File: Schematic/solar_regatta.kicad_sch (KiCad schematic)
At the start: 21 parts, among them M1 24V, SW1 3_Pos_Switch, SW2 Deadman_Switch, SW3 Momentary_Throttle, U1 ESP32-S3, U2 NLSV2T244D

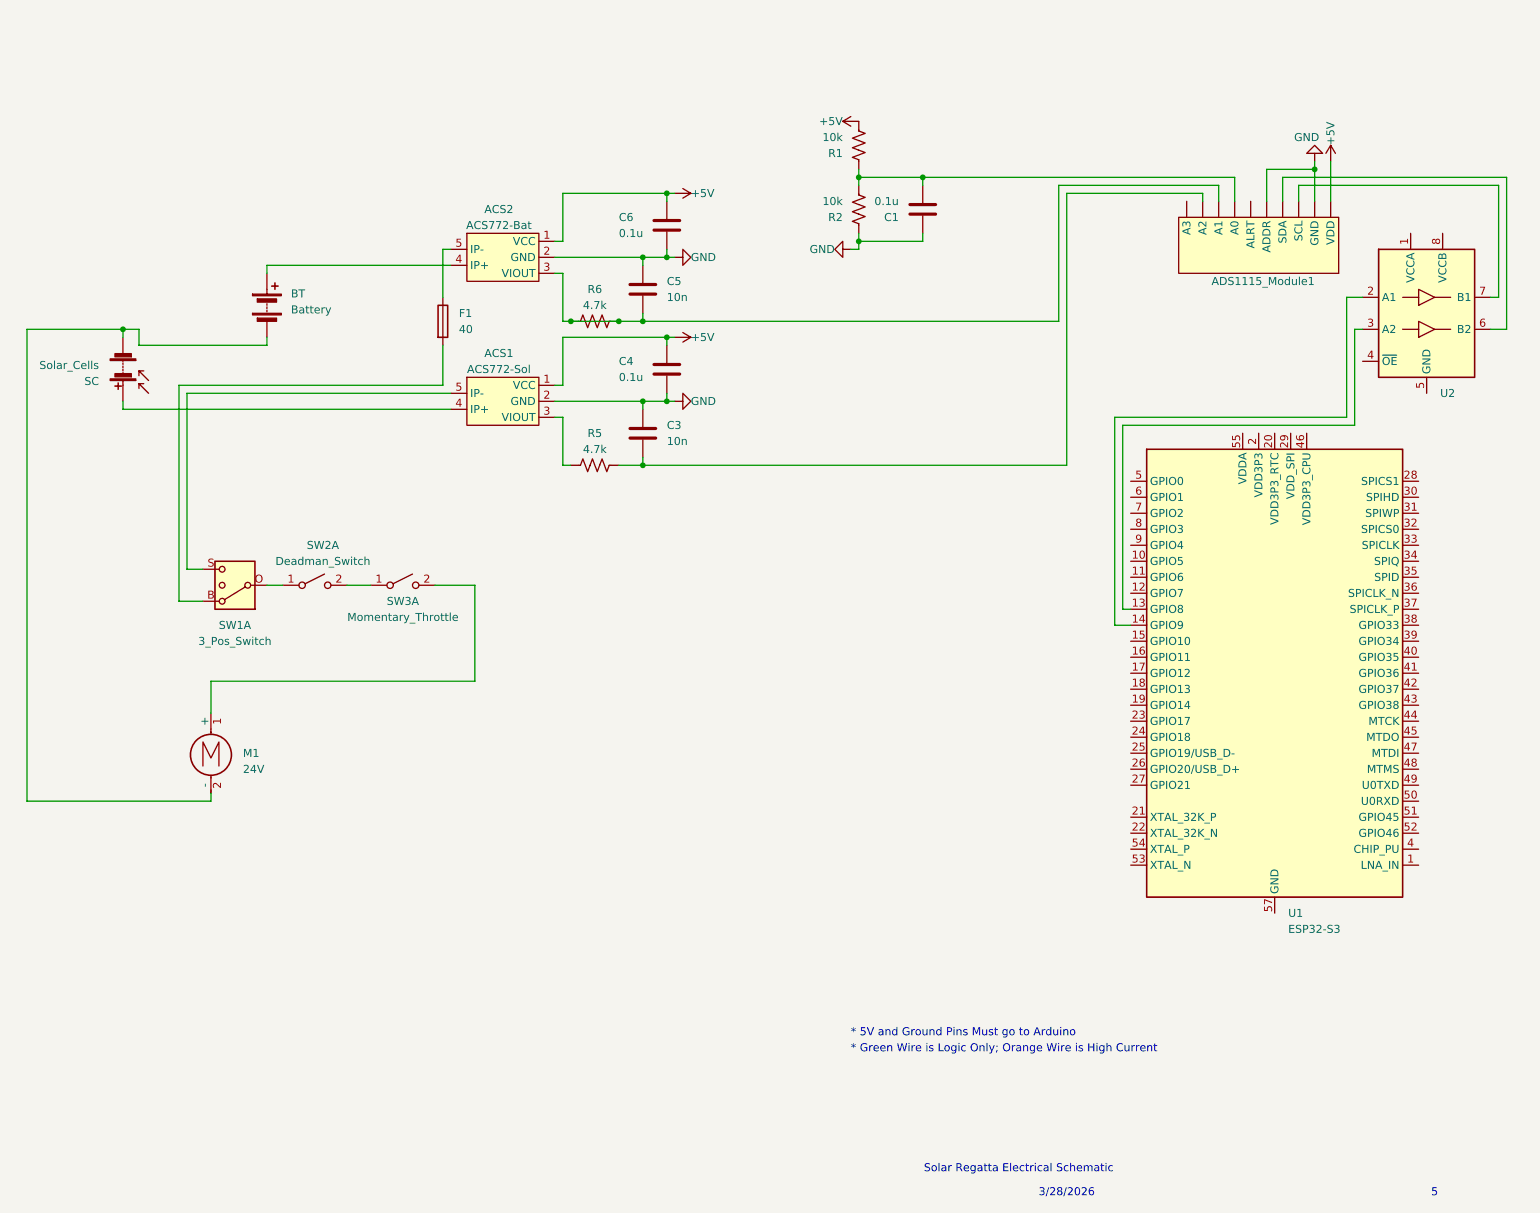
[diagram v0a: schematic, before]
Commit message: Update schematic to include complete esp32 system
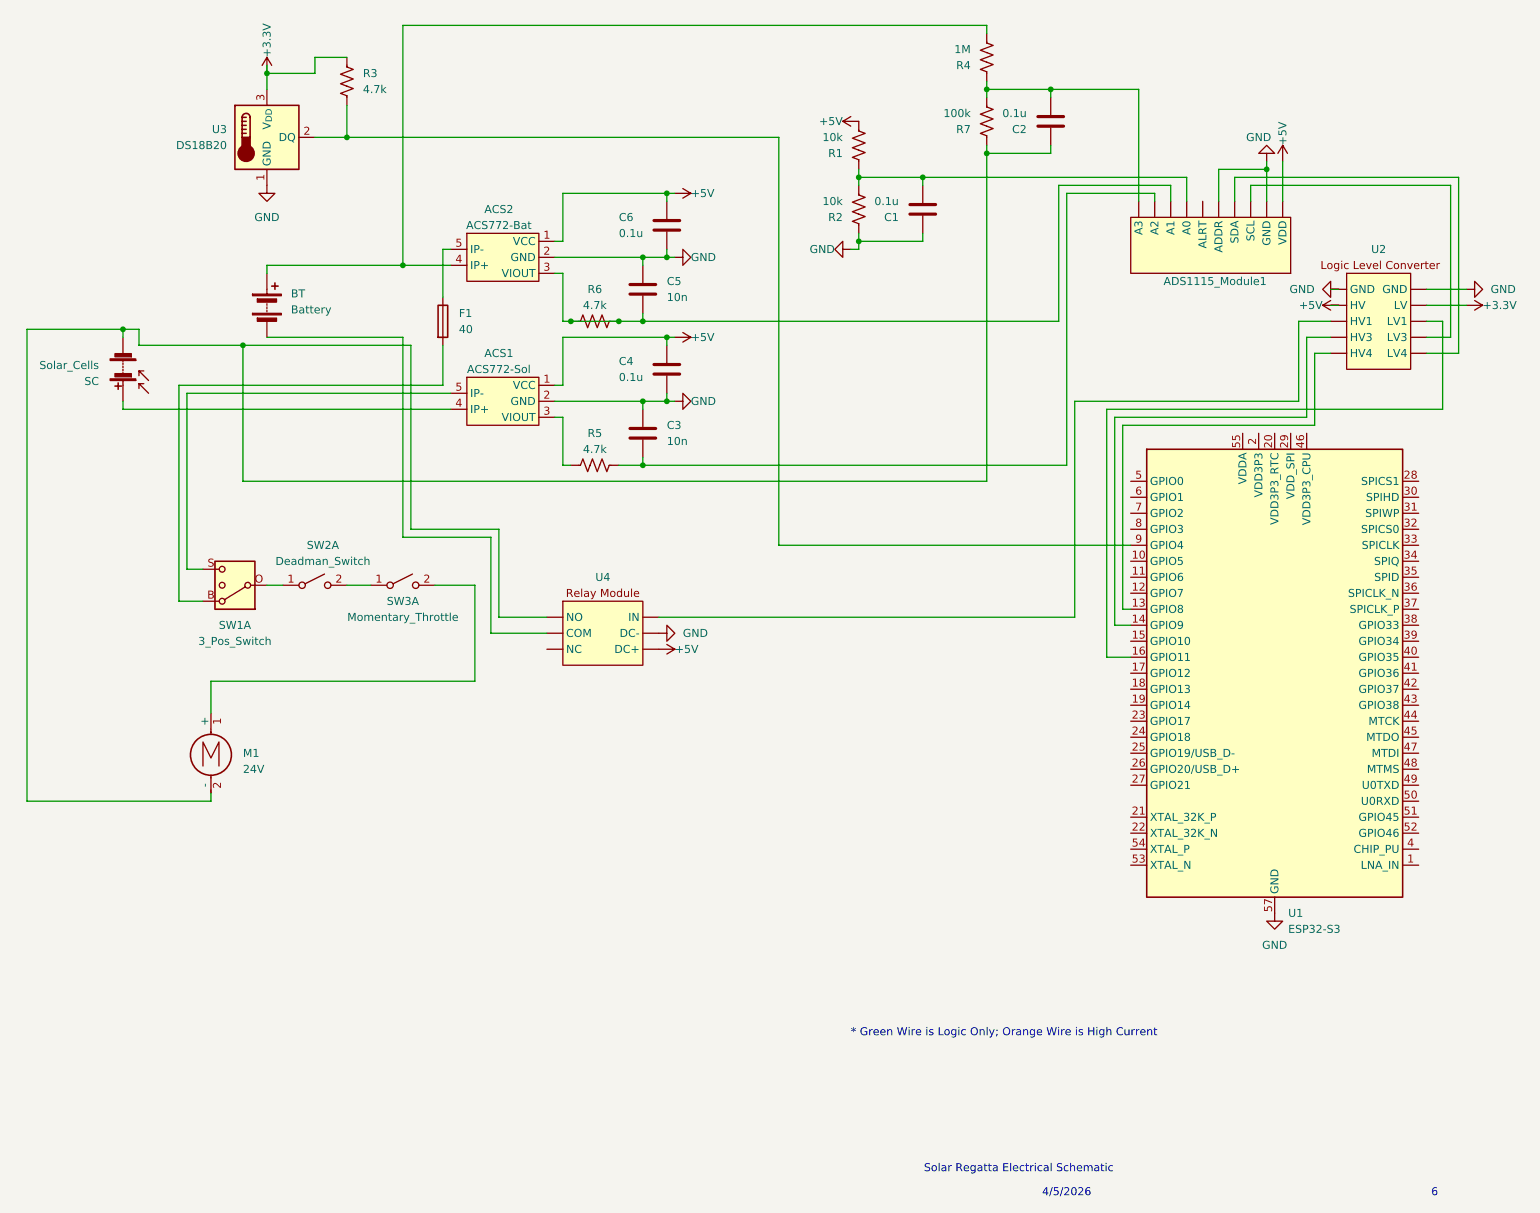
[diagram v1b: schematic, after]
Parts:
- removed U2: NLSV2T244D, Package_SO:SOIC-8_3.9x4.9mm_P1.27mm, symbol Logic_LevelTranslator:NLSV2T244D
- added C2: 0.1u, symbol Device:C
- added R3: 4.7k, symbol Device:R_US
- added R4: 1M, symbol Device:R_US
- added R7: 100k, symbol Device:R_US
- added U2: ~, symbol Custom_Library:LevelConverter
- added U3: DS18B20, Package_TO_SOT_THT:TO-92_Inline, symbol Sensor_Temperature:DS18B20
- added U4: ~, symbol Custom_Library:RelayModule
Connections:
- net +5V: now also U2. (LV4), U4. (DC+)
- net GND: now also U1.57 (GND), U2. (LV4), U3.1 (GND), U4. (DC+)
- net at ACS2.4 (IP+), BT.1 (+): now also R4.2
- net at M1.2 (-), SC.2 (-): now also C2.1, R7.1, U4. (DC+); no longer BT.2 (-)
- net at U1.13 (GPIO8): now also U2. (LV4)
- net at U1.14 (GPIO9): now also U2. (LV4)
- net at U1.16 (GPIO11): now also U2. (LV4)
- net at U1.9 (GPIO4): now also R3.2, U3.2 (DQ)
- new net: BT.2 (-), U4. (DC+)
- new net: ADS1115_Module1. (A3), C2.2, R4.1, R7.2
- new net: U2. (LV4), U4. (DC+)
- new net: ADS1115_Module1. (A3), U2. (LV4) (x2)
- new net +3.3V: R3.1, U2. (LV4), U3.3 (V_{DD})
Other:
- note added: "4/5/2026"
- note added: "6"
- note removed: "* 5V and Ground Pins Must go to Arduino"
- note removed: "3/28/2026"
- note removed: "5"
- moved on the sheet: ADS1115_Module1

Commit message: Remove temp, relays from schematic
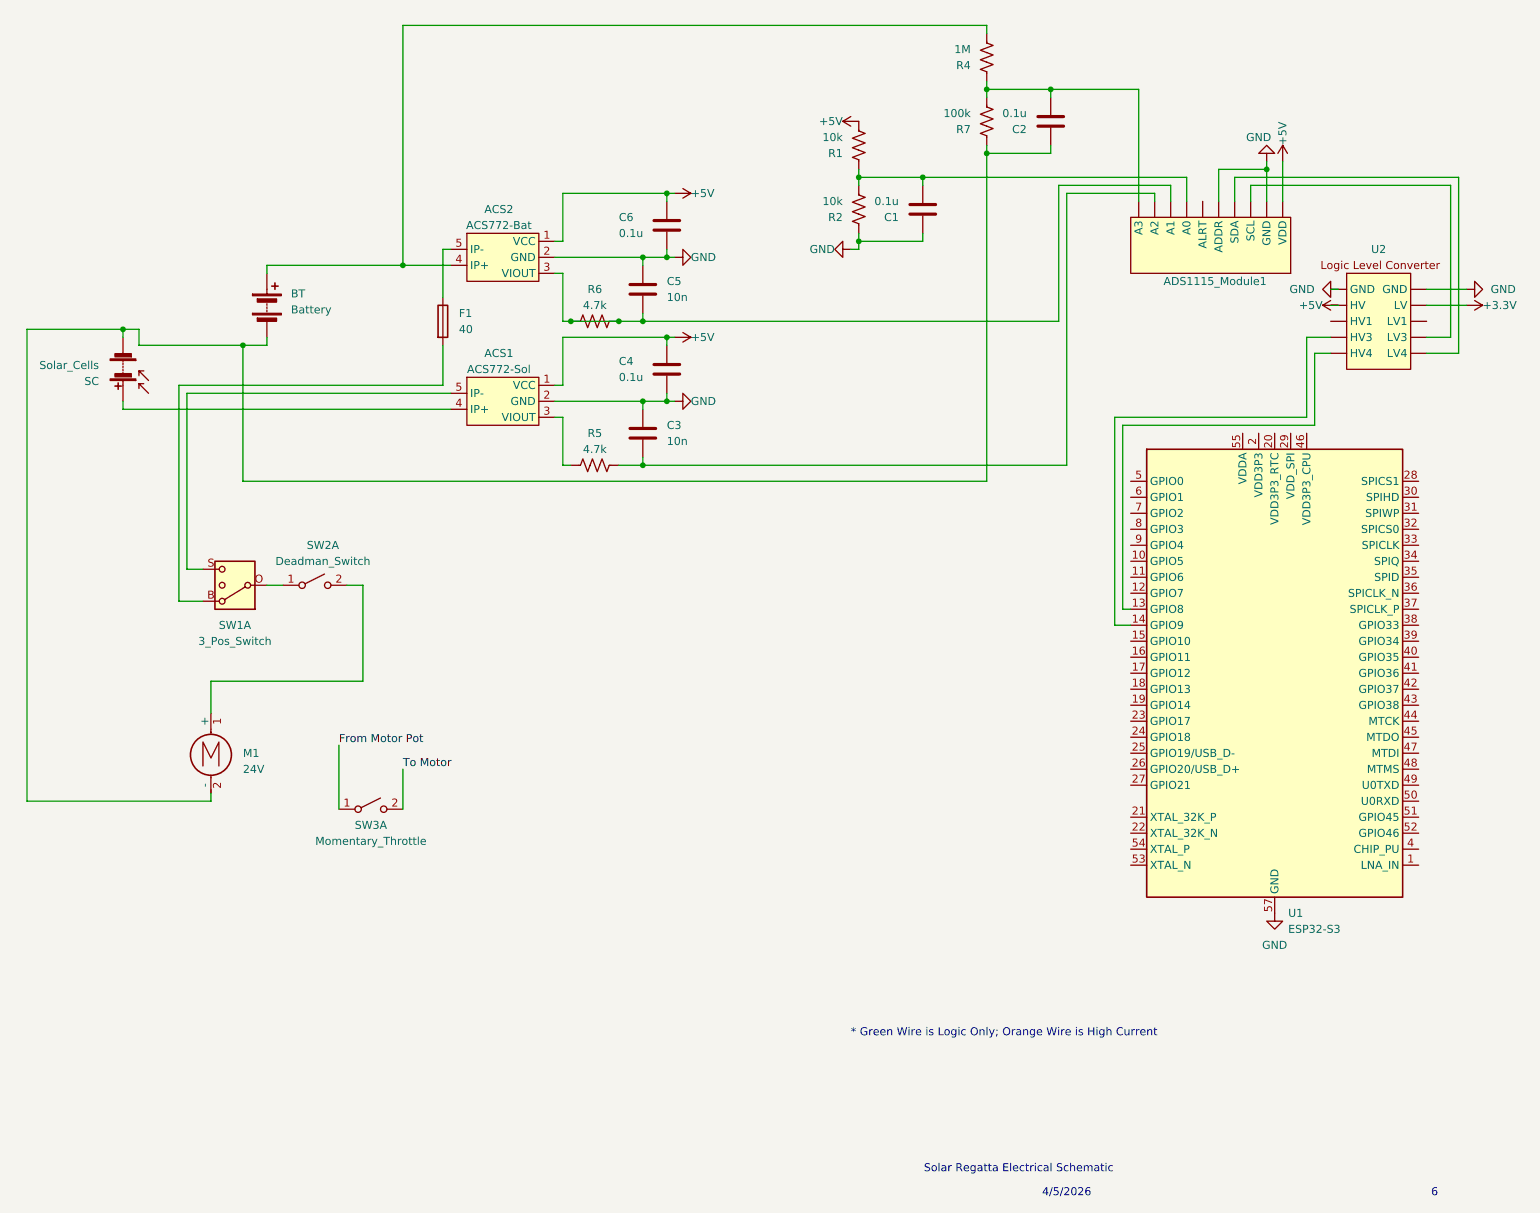
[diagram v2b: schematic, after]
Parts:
- removed R3: 4.7k, symbol Device:R_US
- removed U3: DS18B20, Package_TO_SOT_THT:TO-92_Inline, symbol Sensor_Temperature:DS18B20
- removed U4: ~, symbol Custom_Library:RelayModule
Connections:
- net at BT.2 (-): now also C2.1, M1.2 (-), R7.1, SC.2 (-)
- net at SW2.2 (B): now also M1.1 (+); no longer SW3.1 (A)
- net To Motor: now reaches SW3.2 (B)
- net To Motor: no longer M1.1 (+)
- net at U1.16 (GPIO11): no longer U2. (LV4)
- new net: ADS1115_Module1. (A3), U2. (LV4) (x2)
- new net From Motor Pot: SW3.1 (A)
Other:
- moved on the sheet: SW3A

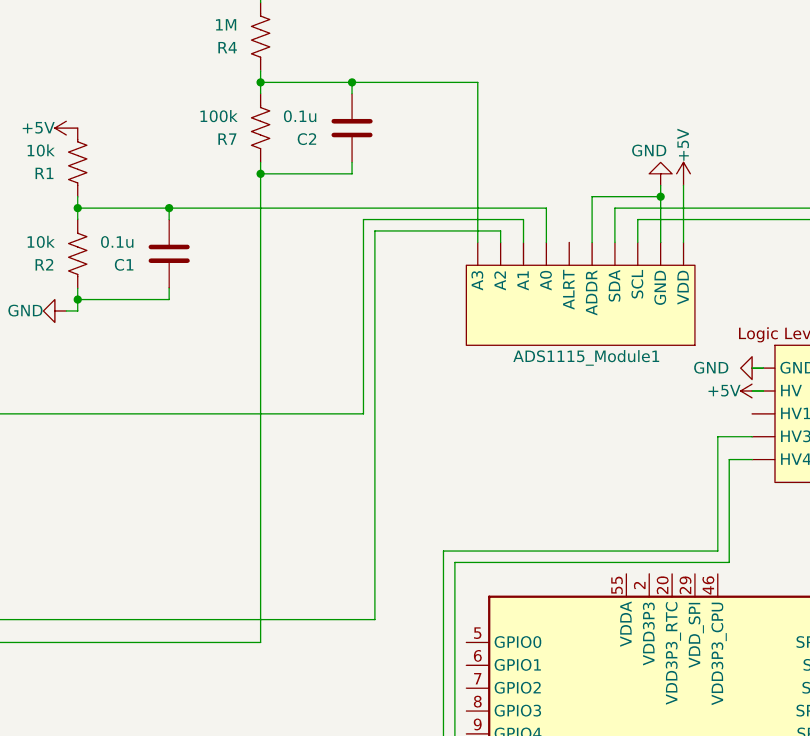
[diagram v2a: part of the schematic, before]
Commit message: Update schematic; Add Models directory
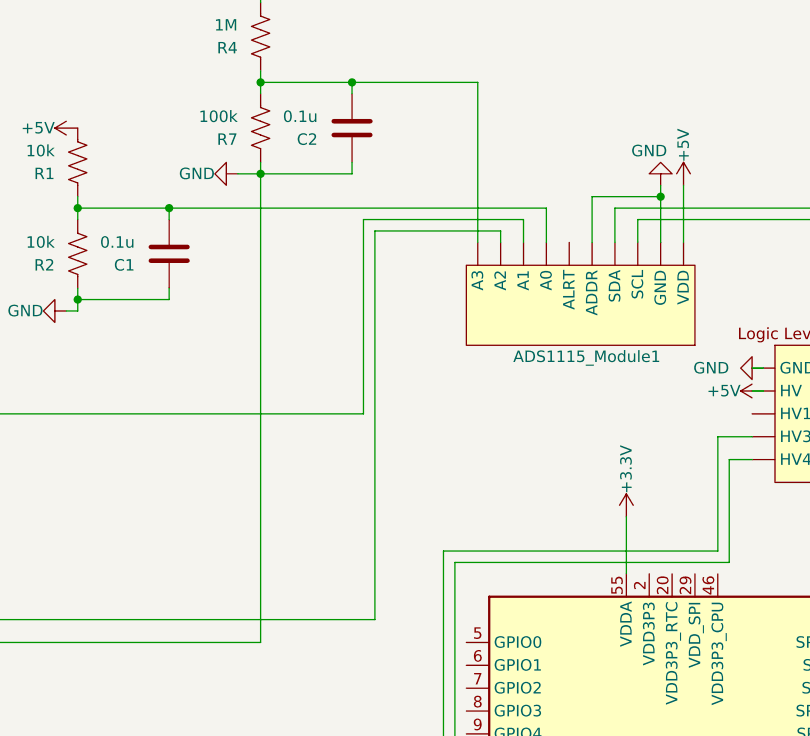
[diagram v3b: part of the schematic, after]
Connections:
- net +3.3V: now also U1.55 (VDDA), U1.56 (VDDA)
- net GND: now also BT.2 (-), C2.1, M1.2 (-), R7.1, SC.2 (-)
- new net: ADS1115_Module1. (A3), U2. (LV4) (x2)
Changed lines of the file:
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@@
 	(wire
 		(pts
-			(xy 130.81 63.5) (xy 132.08 63.5)
-		)
-		(stroke
-			(width 0)
-			(type default)
-		)
-	)
-	(wire
-		(pts
-			(xy 44.45 62.23) (xy 46.99 62.23)
+			(xy 179.07 34.29) (xy 181.61 34.29)
 		)
 		(stroke
@@
 	(wire
 		(pts
-			(xy 161.29 48.26) (xy 171.45 48.26)
+			(xy 130.81 63.5) (xy 132.08 63.5)
 		)
 		(stroke
@@
 	(wire
 		(pts
+			(xy 44.45 62.23) (xy 46.99 62.23)
+		)
+		(stroke
+			(width 0)
+			(type default)
+			(color 204 102 0 1)
+		)
+	)
+	(wire
+		(pts
+			(xy 161.29 48.26) (xy 171.45 48.26)
+		)
+		(stroke
+			(width 0)
+			(type default)
+		)
+	)
+	(wire
+		(pts
 			(xy 130.81 73.66) (xy 127 73.66)
+		)
+		(stroke
+			(width 0)
+			(type default)
+		)
+	)
+	(wire
+		(pts
+			(xy 222.25 72.39) (xy 222.25 78.74)
 		)
 		(stroke
@@
 	)
 	(symbol
+		(lib_id "power:+5V")
+		(at 222.25 72.39 0)
+		(unit 1)
+		(exclude_from_sim no)
+		(in_bom yes)
+		(on_board yes)
+		(dnp no)
+		(property "Reference" "#PWR05"
+			(at 222.25 76.2 0)
+			(effects
+				(font
+					(size 1.27 1.27)
+				)
+				(hide yes)
+			)
+		)
+		(property "Value" "+3.3V"
+			(at 222.25 69.85 90)
+			(effects
+				(font
+					(size 1.27 1.27)
+				)
+				(justify left)
+			)
+		)
+		(property "Footprint" ""
+			(at 222.25 72.39 0)
+			(effects
+				(font
+					(size 1.27 1.27)
+				)
+				(hide yes)
+			)
+		)
+		(property "Datasheet" ""
+			(at 222.25 72.39 0)
+			(effects
+				(font
+					(size 1.27 1.27)
+				)
+				(hide yes)
+			)
+		)
+		(property "Description" "Power symbol creates a global label with name \"+5V\""
+			(at 222.25 72.39 0)
+			(effects
+				(font
+					(size 1.27 1.27)
+				)
+				(hide yes)
+			)
+		)
+		(pin "1"
+		)
+		(instances
+			(project "solar_regatta"
+				(path "/480c4401-87bc-49c2-9123-39a17b8fd968"
+					(reference "#PWR05")
+					(unit 1)
+				)
+			)
+		)
+	)
+	(symbol
 		(lib_id "Switch:SW_DPST_x2")
 		(at 74.93 102.87 0)
@@
 					(unit 1)
 				)
+			)
+		)
+	)
+	(symbol
+		(lib_id "power:GND")
+		(at 179.07 34.29 270)
+		(unit 1)
+		(exclude_from_sim no)
+		(in_bom yes)
+		(on_board yes)
+		(dnp no)
+		(property "Reference" "#PWR06"
+			(at 172.72 34.29 0)
+			(effects
+				(font
+					(size 1.27 1.27)
+				)
+				(hide yes)
+			)
+		)
+		(property "Value" "GND"
+			(at 176.53 34.29 90)
+			(effects
+				(font
+					(size 1.27 1.27)
+				)
+				(justify right)
+			)
+		)
+		(property "Footprint" ""
+			(at 179.07 34.29 0)
+			(effects
+				(font
+					(size 1.27 1.27)
+				)
+				(hide yes)
+			)
+		)
+		(property "Datasheet" ""
+			(at 179.07 34.29 0)
+			(effects
+				(font
+					(size 1.27 1.27)
+				)
+				(hide yes)
+			)
+		)
+		(property "Description" "Power symbol creates a global label with name \"GND\" , ground"
+			(at 179.07 34.29 0)
+			(effects
+				(font
+					(size 1.27 1.27)
+				)
+				(hide yes)
+			)
+		)
+		(pin "1"
+		)
+		(instances
+			(project "solar_regatta"
+				(path "/480c4401-87bc-49c2-9123-39a17b8fd968"
+					(reference "#PWR06")
+					(unit 1)
+				)
